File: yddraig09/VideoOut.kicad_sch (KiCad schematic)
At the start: 37 parts, among them J16 Composite, J17 RGB Video, Q7 2N3904, U46 74HCT04, U47 CXA2075M, Y5 4.4336161875Mhz

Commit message: Some changes
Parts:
- removed C88, C89: 22pF, Capacitor_THT:C_Disc_D5.0mm_W2.5mm_P2.50mm, symbol Device:C
- removed C90, C91, C92: 100nF, Capacitor_THT:C_Disc_D5.0mm_W2.5mm_P2.50mm, symbol Device:C
- removed C93: 47pF, Capacitor_THT:C_Disc_D5.0mm_W2.5mm_P2.50mm, symbol Device:C
- removed C94: 5pF, Capacitor_THT:C_Disc_D5.0mm_W2.5mm_P2.50mm, symbol Device:C
- removed C95, C96, C97, C98: 220uF, Capacitor_THT:CP_Radial_D5.0mm_P2.50mm, symbol Device:C_Polarized
- removed J16: Composite, Ddraig:KLPX0848A2RG, symbol Ddraig:Conn_Coaxial-KLPX0848A2RG
- removed R49, R50, R51: 75R, Resistor_THT:R_Axial_DIN0207_L6.3mm_D2.5mm_P10.16mm_Horizontal, symbol Device:R
- removed R52: 43R, Resistor_THT:R_Axial_DIN0207_L6.3mm_D2.5mm_P10.16mm_Horizontal, symbol Device:R
- removed R54: 240R, Resistor_THT:R_Axial_DIN0207_L6.3mm_D2.5mm_P10.16mm_Horizontal, symbol Device:R
- removed U46: 74HCT04, Package_DIP:DIP-14_W7.62mm_Socket, symbol 74xx:74HCT04
- removed U47: CXA2075M, Package_SO:SOP-24_7.5x15.4mm_P1.27mm, symbol Ddraig:CXA2075M
- removed Y5: 4.4336161875Mhz, Crystal:Crystal_HC50_Vertical, symbol Device:Crystal
- added C104, C90, C92: 220uF, Capacitor_THT:CP_Radial_D6.3mm_P2.50mm, symbol v9958video-rescue:CP-Device
- added C88, C89, C91: 10uF, Capacitor_THT:CP_Radial_D5.0mm_P2.50mm, symbol v9958video-rescue:CP-Device
- added Q10, Q8, Q9: 2N4403, Package_TO_SOT_THT:TO-92, symbol Device:Q_PNP_EBC
- added R18, R60: 100R, rosco_m68k:R-0207_10, symbol Device:R
- added R57: 27K, rosco_m68k:R-0207_10, symbol Device:R
- added R58, R59: 12K, rosco_m68k:R-0207_10, symbol Device:R
- R43: value 4M7 -> 470R
- R44: value 470R -> 27K; footprint Resistor_THT:R_Axial_DIN0207_L6.3mm_D2.5mm_P10.16mm_Horizontal -> rosco_m68k:R-0207_10
- R45: value 470R -> 12K; footprint Resistor_THT:R_Axial_DIN0207_L6.3mm_D2.5mm_P10.16mm_Horizontal -> rosco_m68k:R-0207_10
- R46: value 2K2 -> 100R; footprint Resistor_THT:R_Axial_DIN0207_L6.3mm_D2.5mm_P10.16mm_Horizontal -> rosco_m68k:R-0207_10
- R47: value 2K2 -> 470R
- R48: value 2K81 -> 27K; footprint Resistor_THT:R_Axial_DIN0207_L6.3mm_D2.5mm_P10.16mm_Horizontal -> rosco_m68k:R-0207_10
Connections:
- net PAL_CLK is gone; now on net BLUE: R47.1
- net +5V: now also R44.1, R46.1, R18.1, R57.1, R60.1
- net BLUE: now also C91.1; no longer R42.1
- net BOUT: now also C92.2
- net GND: now also R43.2, R47.2, Q10.3 (C), Q8.3 (C), Q9.3 (C), R58.2, R59.2; no longer R44.2
- net GOUT: now also C90.2
- net GREEN: now also R43.1, C89.1; no longer R44.1
- net RED: now also R42.1, C88.1; no longer R45.1
- net ROUT: now also C104.2
- net ~{CSYNC}: no longer R46.1
- net at R46.2: now also C90.1, Q8.1 (E)
- net at R48.2: now also C91.2, Q10.2 (B), R59.1
- new net: C92.1, Q10.1 (E), R60.2
- new net: C89.2, Q8.2 (B), R44.2, R45.1
- new net: C88.2, Q9.2 (B), R57.2, R58.1
- new net: C104.1, Q9.1 (E), R18.2
- no-connect marks 7 -> 0
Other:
- moved on the sheet: C100, C101, C102, C103, C99, Q7, R42, R53, R55, R56

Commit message: Changing the yddraig09 project
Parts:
- R42, R43, R47: value 470R -> 1K
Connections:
- net BOUT: no longer C92.2, J17.6
- new net: C92.2, J17.6
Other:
- moved on the sheet: C99, J17, Q7, R53, R55, R56

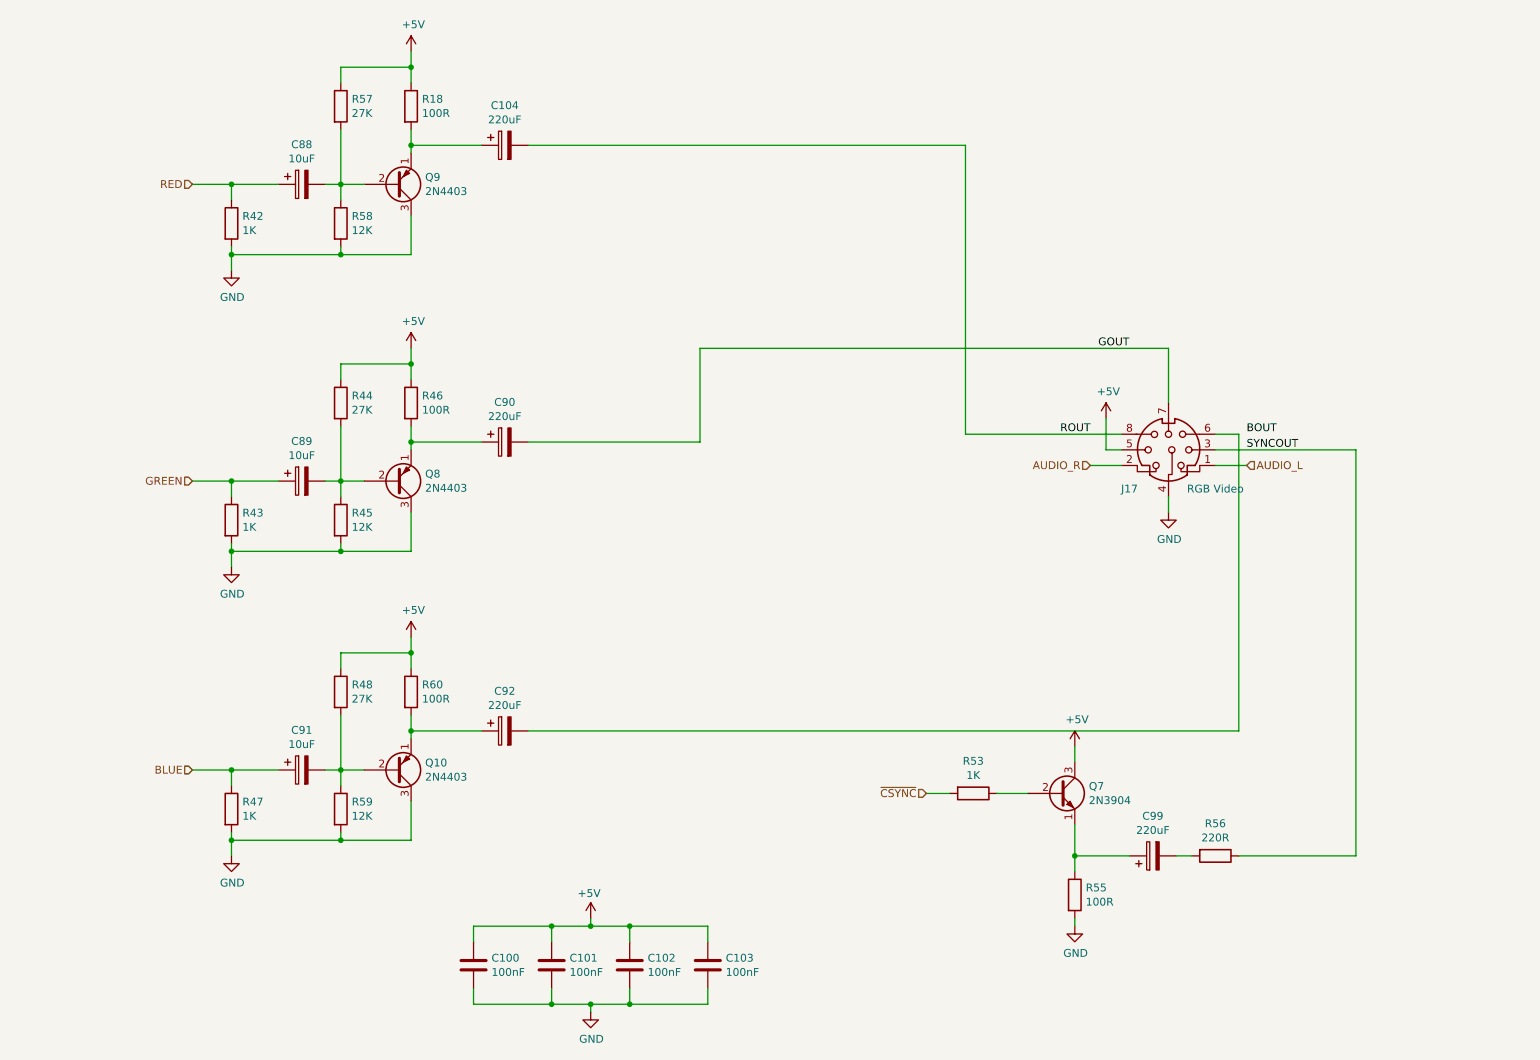
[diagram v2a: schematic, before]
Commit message: Finished changes to 6809 schematics
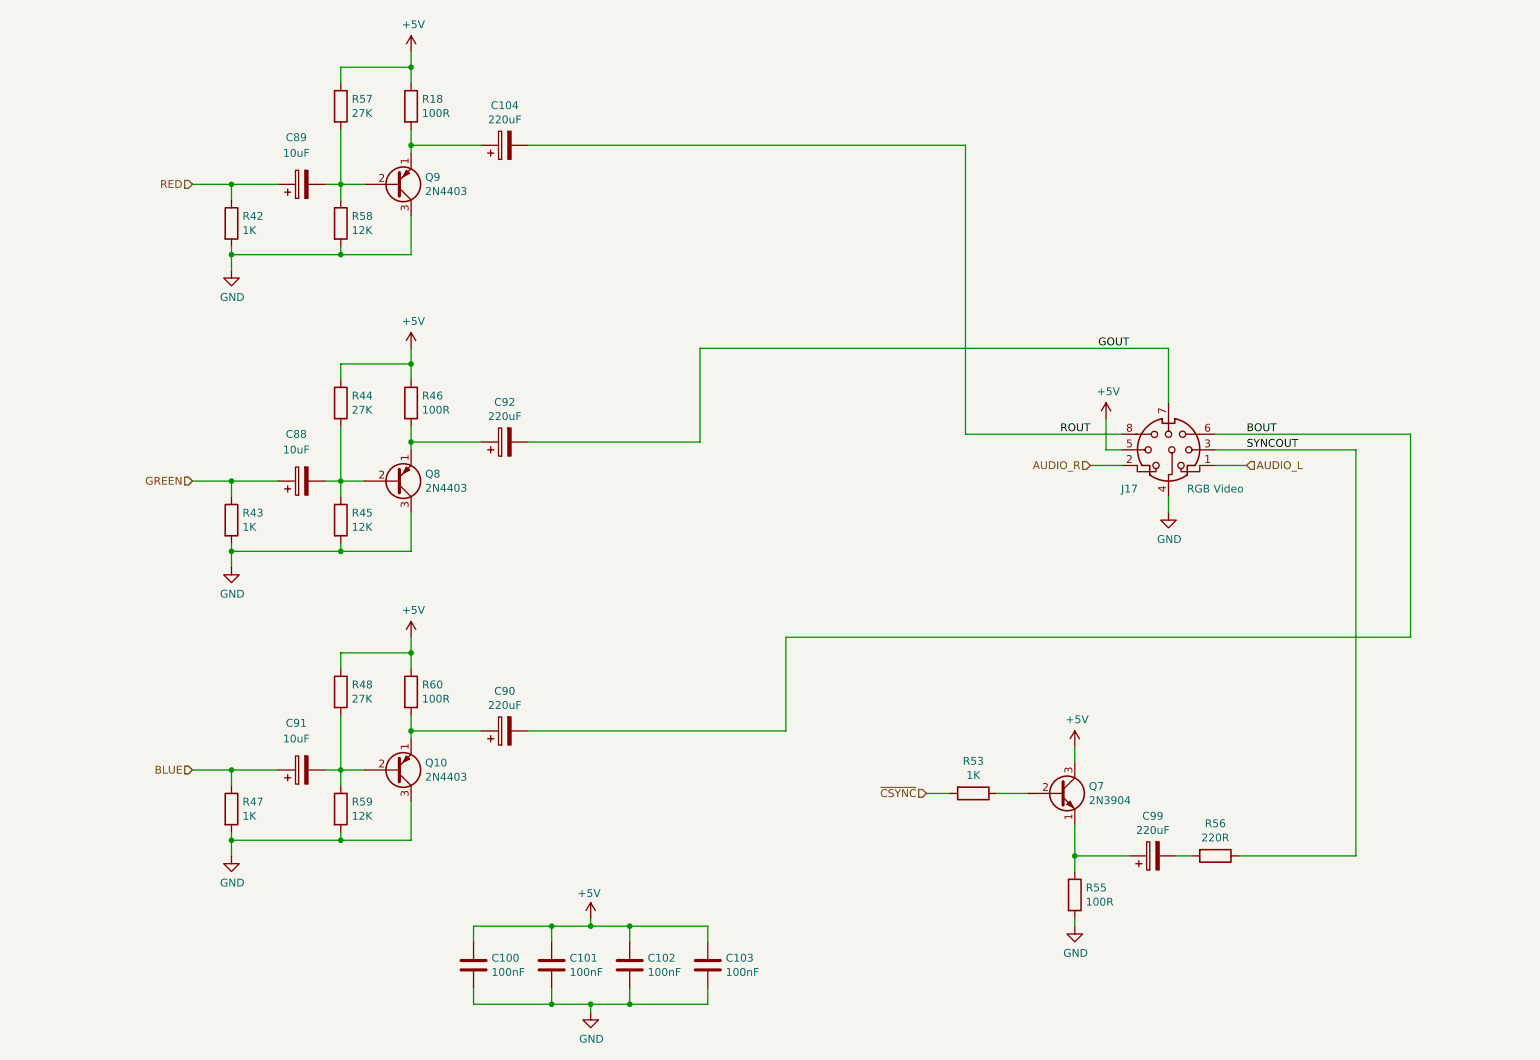
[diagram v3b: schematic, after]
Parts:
- removed C104, C90, C92: 220uF, Capacitor_THT:CP_Radial_D6.3mm_P2.50mm, symbol v9958video-rescue:CP-Device
- removed C88, C89, C91: 10uF, Capacitor_THT:CP_Radial_D5.0mm_P2.50mm, symbol v9958video-rescue:CP-Device
- added C104, C90, C92: 220uF, Capacitor_THT:CP_Radial_D5.0mm_P2.50mm, symbol Device:C_Polarized
- added C88, C89, C91: 10uF, symbol Device:C_Polarized
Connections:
- net BLUE: now also C91.1
- net BOUT: now also J17.6, C90.2
- net GOUT: now also C92.2
- net GREEN: now also C88.1
- net RED: now also C89.1
- net ROUT: now also C104.2
- net at Q10.1 (E), R60.2: now also C90.1
- net at Q10.2 (B), R48.2, R59.1: now also C91.2
- net at Q8.1 (E), R46.2: now also C92.1
- net at Q8.2 (B), R44.2, R45.1: now also C88.2
- net at Q9.2 (B), R57.2, R58.1: now also C89.2
- net at Q9.1 (E), R18.2: now also C104.1

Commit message: 6809 board changes
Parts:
- C85: renamed from C89; footprint (none) -> Capacitor_THT:CP_Radial_D5.0mm_P2.50mm
- C86: renamed from C88; footprint (none) -> Capacitor_THT:CP_Radial_D5.0mm_P2.50mm
- C87: renamed from C91; footprint (none) -> Capacitor_THT:CP_Radial_D5.0mm_P2.50mm
- R47: renamed from R57; footprint rosco_m68k:R-0207_10 -> Resistor_THT:R_Axial_DIN0207_L6.3mm_D2.5mm_P10.16mm_Horizontal
- R48: renamed from R58; footprint rosco_m68k:R-0207_10 -> Resistor_THT:R_Axial_DIN0207_L6.3mm_D2.5mm_P10.16mm_Horizontal
- R49: renamed from R44; footprint rosco_m68k:R-0207_10 -> Resistor_THT:R_Axial_DIN0207_L6.3mm_D2.5mm_P10.16mm_Horizontal
- R50: renamed from R45; footprint rosco_m68k:R-0207_10 -> Resistor_THT:R_Axial_DIN0207_L6.3mm_D2.5mm_P10.16mm_Horizontal
- R51: renamed from R48; footprint rosco_m68k:R-0207_10 -> Resistor_THT:R_Axial_DIN0207_L6.3mm_D2.5mm_P10.16mm_Horizontal
- R52: renamed from R59; footprint rosco_m68k:R-0207_10 -> Resistor_THT:R_Axial_DIN0207_L6.3mm_D2.5mm_P10.16mm_Horizontal
- R53: renamed from R18; footprint rosco_m68k:R-0207_10 -> Resistor_THT:R_Axial_DIN0207_L6.3mm_D2.5mm_P10.16mm_Horizontal
- R54: renamed from R46; footprint rosco_m68k:R-0207_10 -> Resistor_THT:R_Axial_DIN0207_L6.3mm_D2.5mm_P10.16mm_Horizontal
- R55: renamed from R60; footprint rosco_m68k:R-0207_10 -> Resistor_THT:R_Axial_DIN0207_L6.3mm_D2.5mm_P10.16mm_Horizontal
- renumbered C100 to C88, C104 to C89, C92 to C90, C90 to C91, C101 to C92, C102 to C93, C103 to C94, C99 to C95, J17 to J14, Q7 to Q10, Q9 to Q7, Q10 to Q9, R42 to R44, R43 to R45, R47 to R46, R53 to R56, R55 to R57, R56 to R58

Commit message: Changes to yddraig09
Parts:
- removed C88, C94: 100nF, Capacitor_THT:C_Disc_D5.0mm_W2.5mm_P2.50mm, symbol Device:C
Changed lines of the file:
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@@
-	)
-	(junction
-		(at 129.54 170.18)
-		(diameter 0)
-		(color 0 0 0 0)
-	)
-	(junction
-		(at 116.84 170.18)
-		(diameter 0)
-		(color 0 0 0 0)
 	)
 	(junction
@@
 	)
 	(junction
-		(at 116.84 182.88)
-		(diameter 0)
-		(color 0 0 0 0)
-	)
-	(junction
 		(at 93.98 78.74)
 		(diameter 0)
@@
 	)
 	(junction
-		(at 129.54 182.88)
-		(diameter 0)
-		(color 0 0 0 0)
-	)
-	(junction
 		(at 82.55 109.22)
 		(diameter 0)
@@
 	(wire
 		(pts
-			(xy 129.54 170.18) (xy 142.24 170.18)
-		)
-		(stroke
-			(width 0)
-			(type default)
-		)
-	)
-	(wire
-		(pts
 			(xy 113.03 138.43) (xy 154.94 138.43)
 		)
@@
 	(wire
 		(pts
-			(xy 104.14 172.72) (xy 104.14 170.18)
-		)
-		(stroke
-			(width 0)
-			(type default)
-		)
-	)
-	(wire
-		(pts
 			(xy 210.82 158.75) (xy 201.93 158.75)
 		)
@@
 	(wire
 		(pts
-			(xy 104.14 170.18) (xy 116.84 170.18)
-		)
-		(stroke
-			(width 0)
-			(type default)
-		)
-	)
-	(wire
-		(pts
 			(xy 82.55 144.78) (xy 86.36 144.78)
 		)
@@
 	(wire
 		(pts
-			(xy 142.24 182.88) (xy 142.24 180.34)
-		)
-		(stroke
-			(width 0)
-			(type default)
-		)
-	)
-	(wire
-		(pts
 			(xy 93.98 123.19) (xy 93.98 125.73)
 		)
@@
 	(wire
 		(pts
-			(xy 129.54 182.88) (xy 142.24 182.88)
-		)
-		(stroke
-			(width 0)
-			(type default)
-		)
-	)
-	(wire
-		(pts
 			(xy 224.79 92.71) (xy 247.65 92.71)
 		)
@@
 	(wire
 		(pts
-			(xy 104.14 180.34) (xy 104.14 182.88)
-		)
-		(stroke
-			(width 0)
-			(type default)
-		)
-	)
-	(wire
-		(pts
 			(xy 82.55 125.73) (xy 93.98 125.73)
 		)
@@
 	(wire
 		(pts
-			(xy 142.24 170.18) (xy 142.24 172.72)
-		)
-		(stroke
-			(width 0)
-			(type default)
-		)
-	)
-	(wire
-		(pts
 			(xy 220.98 158.75) (xy 218.44 158.75)
 		)
@@
 		(pts
 			(xy 82.55 49.53) (xy 80.01 49.53)
-		)
-		(stroke
-			(width 0)
-			(type default)
-		)
-	)
-	(wire
-		(pts
-			(xy 104.14 182.88) (xy 116.84 182.88)
 		)
 		(stroke
@@
 			)
 			(justify right)
-		)
-	)
-	(symbol
-		(lib_id "Device:C")
-		(at 104.14 176.53 0)
-		(unit 1)
-		(exclude_from_sim no)
-		(in_bom yes)
-		(on_board yes)
-		(dnp no)
-		(property "Reference" "C88"
-			(at 107.061 175.3616 0)
-			(effects
-				(font
-					(size 1.27 1.27)
-				)
-				(justify left)
-			)
-		)
-		(property "Value" "100nF"
-			(at 107.061 177.673 0)
-			(effects
-				(font
-					(size 1.27 1.27)
-				)
-				(justify left)
-			)
-		)
-		(property "Footprint" "Capacitor_THT:C_Disc_D5.0mm_W2.5mm_P2.50mm"
-			(at 105.1052 180.34 0)
-			(effects
-				(font
-					(size 1.27 1.27)
-				)
-				(hide yes)
-			)
-		)
-		(property "Datasheet" "~"
-			(at 104.14 176.53 0)
-			(effects
-				(font
-					(size 1.27 1.27)
-				)
-				(hide yes)
-			)
-		)
-		(property "Description" "Unpolarized capacitor"
-			(at 104.14 176.53 0)
-			(effects
-				(font
-					(size 1.27 1.27)
-				)
-				(hide yes)
-			)
-		)
-		(pin "1"
-		)
-		(pin "2"
-		)
-		(instances
-			(project "yddraig09"
-				(path "/3cf18d79-3df5-467d-a147-795d8b124c26/00000000-0000-0000-0000-0000619d3c4f"
-					(reference "C88")
-					(unit 1)
-				)
-			)
 		)
 	)
@@
 				)
 				(justify left)
+				(hide yes)
 			)
 		)
@@
 					(unit 1)
 				)
-			)
-		)
-	)
-	(symbol
-		(lib_id "Device:C")
-		(at 142.24 176.53 0)
-		(unit 1)
-		(exclude_from_sim no)
-		(in_bom yes)
-		(on_board yes)
-		(dnp no)
-		(property "Reference" "C94"
-			(at 145.161 175.3616 0)
-			(effects
-				(font
-					(size 1.27 1.27)
-				)
-				(justify left)
-			)
-		)
-		(property "Value" "100nF"
-			(at 145.161 177.673 0)
-			(effects
-				(font
-					(size 1.27 1.27)
-				)
-				(justify left)
-			)
-		)
-		(property "Footprint" "Capacitor_THT:C_Disc_D5.0mm_W2.5mm_P2.50mm"
-			(at 143.2052 180.34 0)
-			(effects
-				(font
-					(size 1.27 1.27)
-				)
-				(hide yes)
-			)
-		)
-		(property "Datasheet" "~"
-			(at 142.24 176.53 0)
-			(effects
-				(font
-					(size 1.27 1.27)
-				)
-				(hide yes)
-			)
-		)
-		(property "Description" "Unpolarized capacitor"
-			(at 142.24 176.53 0)
-			(effects
-				(font
-					(size 1.27 1.27)
-				)
-				(hide yes)
-			)
-		)
-		(pin "1"
-		)
-		(pin "2"
-		)
-		(instances
-			(project "yddraig09"
-				(path "/3cf18d79-3df5-467d-a147-795d8b124c26/00000000-0000-0000-0000-0000619d3c4f"
-					(reference "C94")
-					(unit 1)
-				)

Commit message: BOard changes
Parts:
- renumbered C85 to C84, C86 to C85, C87 to C86, C89 to C87, C90 to C88, C91 to C89, C92 to C90, C93 to C91, C95 to C92, Q7 to Q5, Q8 to Q6, Q9 to Q7, Q10 to Q8, R44 to R41, R45 to R42, R46 to R43, R47 to R44, R48 to R45, R49 to R46, R50 to R47, R51 to R48, R52 to R49, R53 to R50, R54 to R51, R55 to R52, R56 to R53, R57 to R54, R58 to R55
